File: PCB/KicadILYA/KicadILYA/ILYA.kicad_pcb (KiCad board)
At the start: 2 copper layers, 6 parts, among them U1 NodeMCU1.0(ESP-12E), U101 Temperature_connector, U102 Pin-SocketESP8266_1x15_2, U103 Pin-SocketESP8266_1x15, U2 Relay_2_pins, U3101 Flow_connector

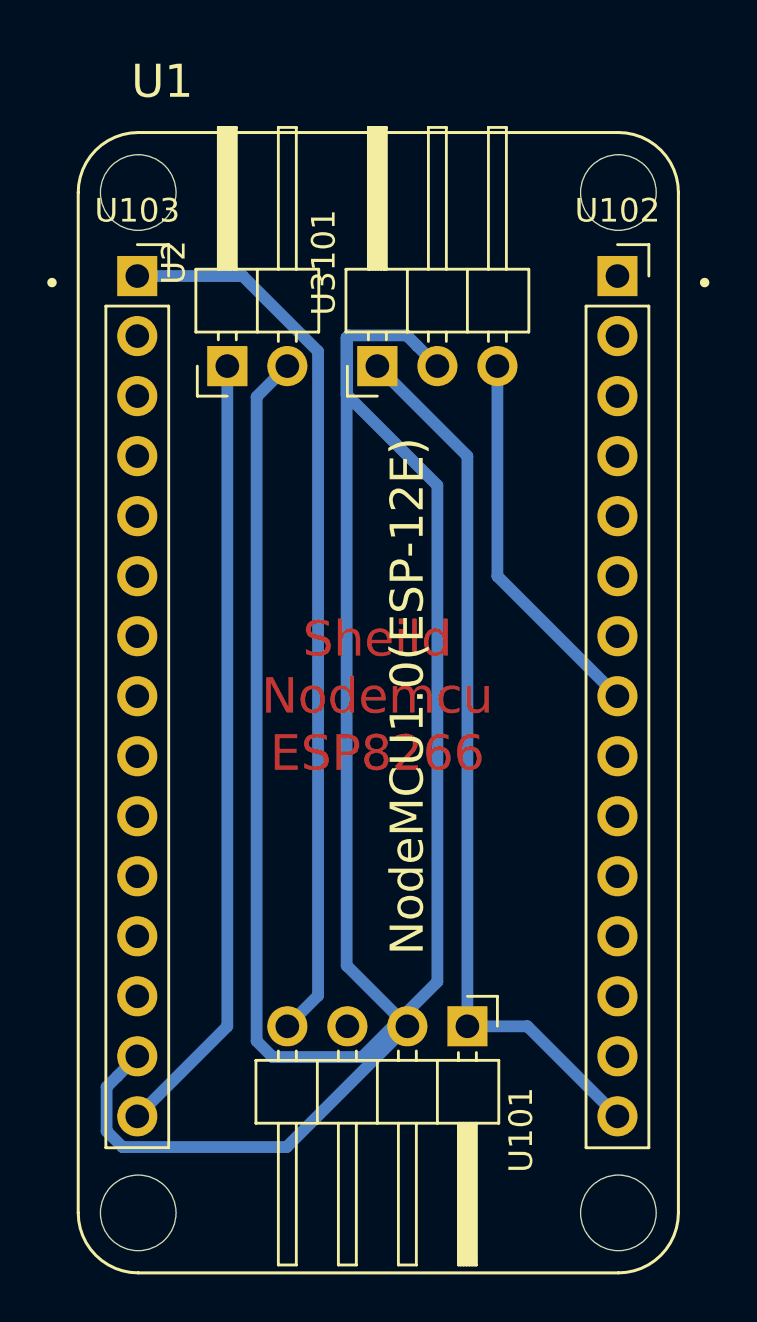
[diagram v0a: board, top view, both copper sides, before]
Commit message: Correction of tracks size
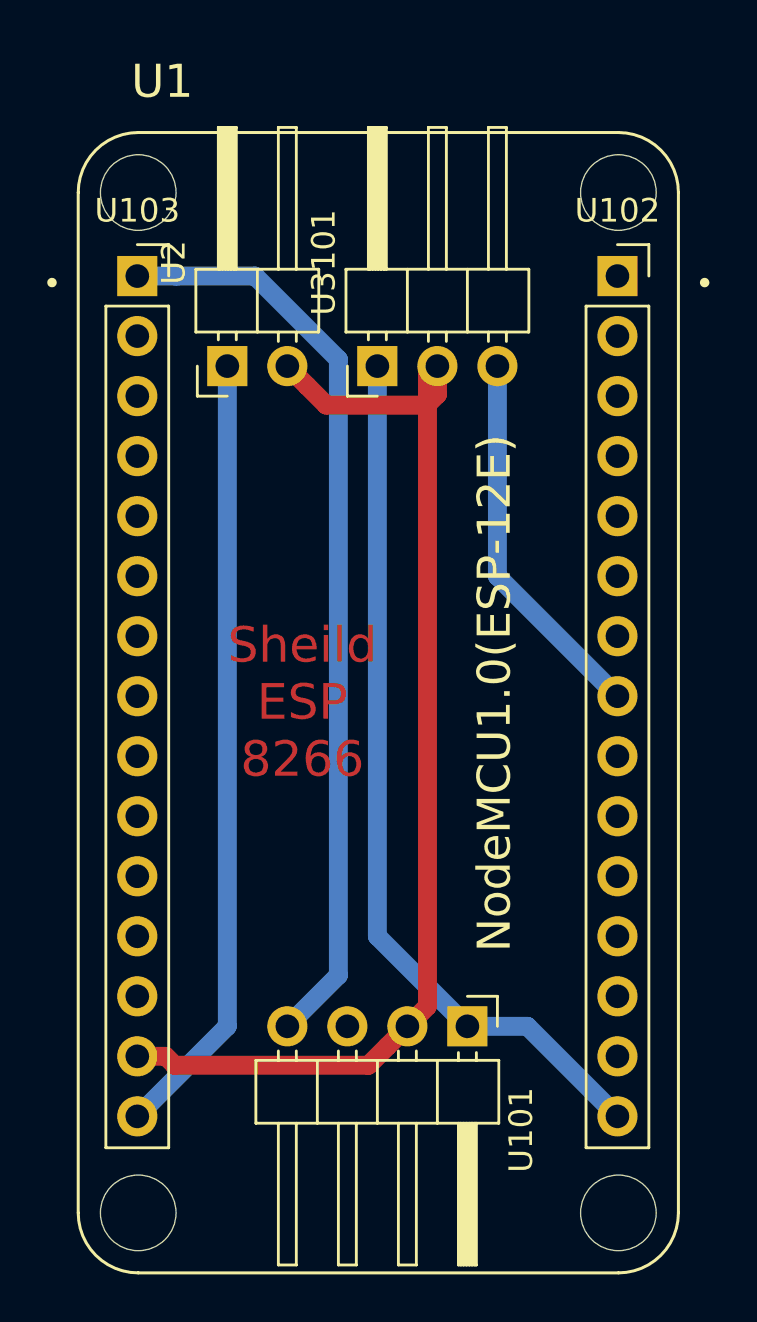
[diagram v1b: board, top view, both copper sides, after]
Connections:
- net VCC renamed +3V3
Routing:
- net GND: track 120.7 -> 49.2 mm
- net SIGtemp: track 38.1 -> 39.1 mm
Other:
- net class Default: clearance 0.2 -> 0.4; trace_width 0.25 -> 0.8; via_dia 0.8 -> 1.6; via_drill 0.4 -> 0.8
- rule trace_clearance: 0.2 -> 0.4
- board text added: "Sheild ESP 8266"
- board text removed: "Sheild Nodemcu ESP8266"
